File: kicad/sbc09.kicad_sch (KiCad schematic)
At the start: 77 parts, among them J1 Conn_01x04_Male, J2 Conn_01x06_Male, J3 Conn_01x06_Male, J4 Conn_01x06_Male, J5 Conn_02x05_Odd_Even, J6 Conn_02x25_Odd_Even, J7 Conn_02x05_Odd_Even, Q1 2N7000, SW1 SW_Push, U1 74HCT245, U10 SST39SF040-DIP, U11 XR68C681CJ, U12 MAX232, U2 74HCT245, U3 74HCT245, U4 MC6809E, U5 74HCT125, U6 EPM7128SLC84, U7 71256SA15TPG, U8 AS6C4008-55PCN, U9 SST39SF040-DIP, X1 8MHz, X2 3.6864MHz

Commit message: KiCAD: Replace 74HCT125 with 74HCT32 and add INTMASK from CPLD
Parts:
- removed U5: 74HCT125, Package_DIP:DIP-14_W7.62mm_Socket, symbol 74xx:74LS125
- added U5: 74HCT32, Package_DIP:DIP-14_W7.62mm_Socket, symbol 74xx:74LS32
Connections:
- net A3: no longer U6.21 (A3)
- net CLKX4: now also U5.4
- net CLKX4Bus: now also U5.6
- net E: now also U6.8 (EX), U5.1
- net EBus: now also U5.3
- net GND: now also U5.2, U5.5, U5.7 (GND)
- net Q: now also U6.5 (QX)
- net VCC: now also U5.14 (VCC)
- net nENCLK: now also U6.6 (ENCLK)
- net nFIRQ: now also U5.13; no longer U4.4 (~{FIRQ})
- net nIRQ: now also U5.9; no longer U4.3 (~{IRQ})
- new net: U4.4 (~{FIRQ}), U5.11
- new net: U4.3 (~{IRQ}), U5.8
- new net INTMASK: U5.10, U5.12, U6.21 (INTMASK)
- no-connect marks 22 -> 21
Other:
- note added: "NOTE: Could save a pin by combining EX and E."
- moved on the sheet: RN1

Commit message: KiCAD: Connect SD Card to CPLD
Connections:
- net GND: now also U7.3 (A7), U7.4 (A6), U7.5 (A5)
- net SDCLK: now also U6.73 (SCLK); no longer U11.29 (OP6)
- net SDCS: now also U11.17 (OP7); no longer U11.16 (OP5)
- net SDMISO: now also U6.74 (MISO); no longer U11.42 (IP5)
- net SDMOSI: now also U6.76 (MOSI); no longer U11.17 (OP7)
- removed net MMU_A5: U6.73 (MMU_A5), U7.5 (A5)
- removed net MMU_A6: U6.76 (MMU_A6), U7.4 (A6)
- removed net MMU_A7: U6.74 (MMU_A7), U7.3 (A7)
- no-connect marks 21 -> 24
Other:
- moved on the sheet: J4

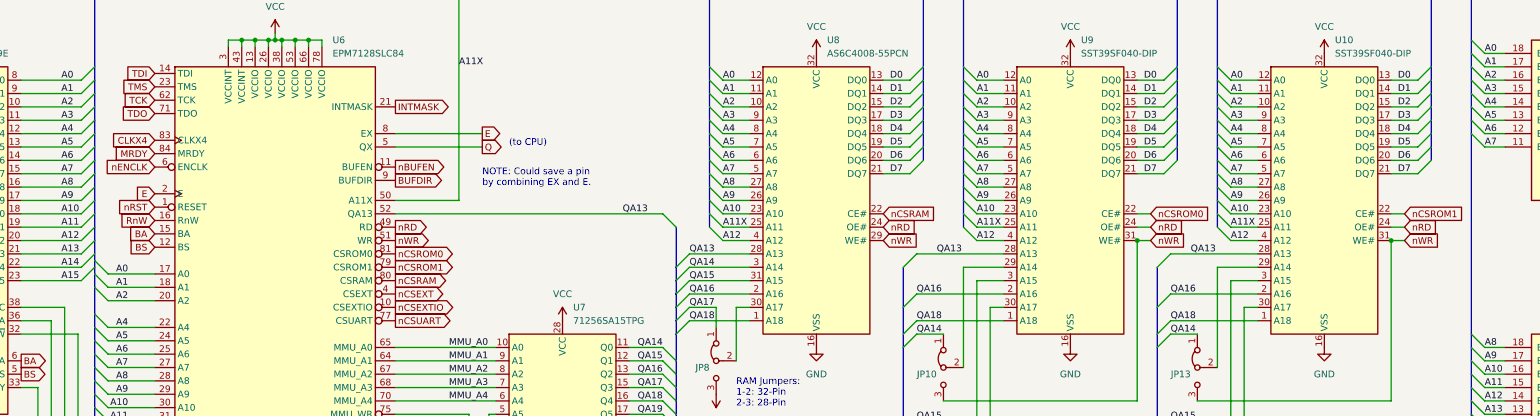
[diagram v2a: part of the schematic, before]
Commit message: KiCAD: Re-instate ADDR3 at the expense of seperate nRD/nWR signals
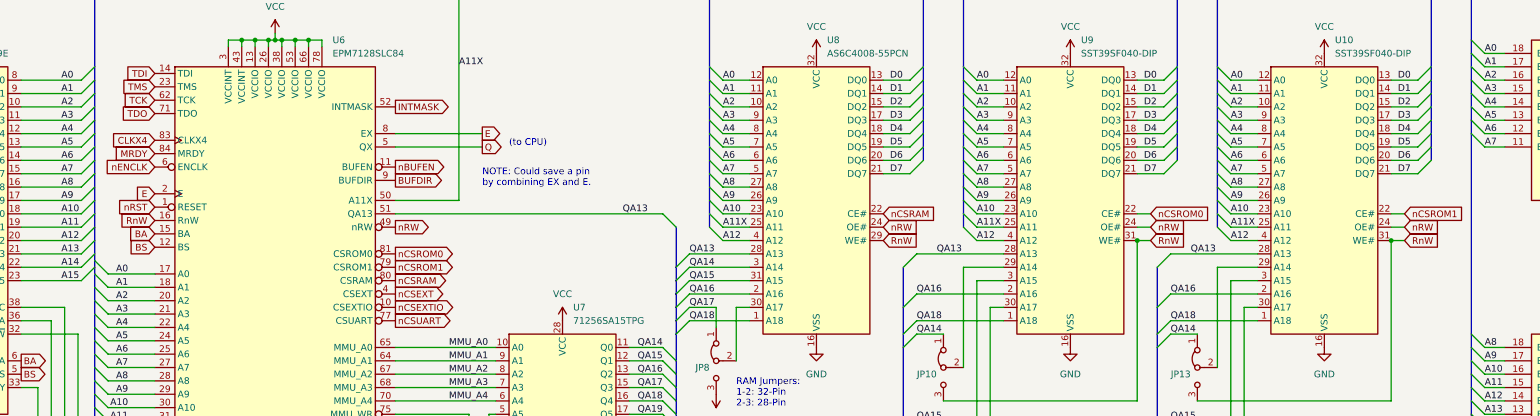
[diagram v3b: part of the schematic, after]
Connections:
- net A3: now also U6.21 (A3)
- net INTMASK: now also U6.52 (INTMASK); no longer U6.21 (INTMASK)
- net QA13: now also U6.51 (QA13); no longer U6.52 (QA13)
- net RnW: now also JP10.3 (B), JP13.3 (B), U10.31 (WE#), U8.29 (WE#), U9.31 (WE#)
- net nRD renamed nRW
- removed net nWR: JP10.3 (B), JP13.3 (B), U10.31 (WE#), U6.51 (WR), U8.29 (WE#), U9.31 (WE#)
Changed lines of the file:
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@@
     (stroke (width 0) (type default) (color 0 0 0 0))
   )
+  (bus_entry (at 93.98 85.09) (size -2.54 -2.54)
+    (stroke (width 0) (type default) (color 0 0 0 0))
+  )
   (bus_entry (at 201.93 76.2) (size 2.54 -2.54)
     (stroke (width 0) (type default) (color 0 0 0 0))
@@
     (stroke (width 0) (type default) (color 0 0 0 0))
   )
+  (wire (pts (xy 93.98 85.09) (xy 102.87 85.09))
+    (stroke (width 0) (type default) (color 0 0 0 0))
+  )
   (wire (pts (xy 77.47 40.64) (xy 88.9 40.64))
     (stroke (width 0) (type default) (color 0 0 0 0))
@@
     (stroke (width 0) (type default) (color 0 0 0 0))
   )
-  (bus (pts (xy 91.44 80.01) (xy 91.44 85.09))
+  (bus (pts (xy 91.44 80.01) (xy 91.44 82.55))
     (stroke (width 0) (type default) (color 0 0 0 0))
   )
@@
     (stroke (width 0) (type default) (color 0 0 0 0))
   )
+  (bus (pts (xy 91.44 82.55) (xy 91.44 85.09))
+    (stroke (width 0) (type default) (color 0 0 0 0))
+  )
   (wire (pts (xy 45.72 53.34) (xy 52.07 53.34))
     (stroke (width 0) (type default) (color 0 0 0 0))
@@
     (effects (font (size 1.27 1.27)) (justify left bottom))
   )
+  (label "A3" (at 97.79 85.09 180)
+    (effects (font (size 1.27 1.27)) (justify right bottom))
+  )
   (label "A6" (at 307.34 55.88 0)
     (effects (font (size 1.27 1.27)) (justify left bottom))
@@
     )
   )
-  (global_label "nWR" (shape input) (at 340.36 71.12 0) (fields_autoplaced)
+  (global_label "RnW" (shape input) (at 340.36 71.12 0) (fields_autoplaced)
     (effects (font (size 1.27 1.27)) (justify left))
     (property "Intersheet References" "${INTERSHEET_REFS}" (id 0) (at 346.6436 71.0406 0)
@@
     )
   )
-  (global_label "nRD" (shape output) (at 148.59 68.58 0) (fields_autoplaced)
+  (global_label "nRW" (shape output) (at 148.59 68.58 0) (fields_autoplaced)
     (effects (font (size 1.27 1.27)) (justify left))
-    (property "Intersheet References" "${INTERSHEET_REFS}" (id 0) (at 154.6921 68.5006 0)
+    (property "Intersheet References" "${INTERSHEET_REFS}" (id 0) (at 154.8736 68.5006 0)
       (effects (font (size 1.27 1.27)) (justify left) hide)
     )
@@
     )
   )
-  (global_label "nRD" (shape input) (at 292.1 68.58 0) (fields_autoplaced)
+  (global_label "nRW" (shape input) (at 292.1 68.58 0) (fields_autoplaced)
     (effects (font (size 1.27 1.27)) (justify left))
-    (property "Intersheet References" "${INTERSHEET_REFS}" (id 0) (at 298.2021 68.5006 0)
+    (property "Intersheet References" "${INTERSHEET_REFS}" (id 0) (at 298.3836 68.5006 0)
       (effects (font (size 1.27 1.27)) (justify left) hide)
     )
@@
     )
   )
-  (global_label "nRD" (shape input) (at 340.36 68.58 0) (fields_autoplaced)
+  (global_label "nRW" (shape input) (at 340.36 68.58 0) (fields_autoplaced)
     (effects (font (size 1.27 1.27)) (justify left))
-    (property "Intersheet References" "${INTERSHEET_REFS}" (id 0) (at 346.4621 68.5006 0)
+    (property "Intersheet References" "${INTERSHEET_REFS}" (id 0) (at 346.6436 68.5006 0)
       (effects (font (size 1.27 1.27)) (justify left) hide)
     )
@@
     )
   )
-  (global_label "nRD" (shape input) (at 241.3 68.58 0) (fields_autoplaced)
+  (global_label "nRW" (shape input) (at 241.3 68.58 0) (fields_autoplaced)
     (effects (font (size 1.27 1.27)) (justify left))
-    (property "Intersheet References" "${INTERSHEET_REFS}" (id 0) (at 247.4021 68.5006 0)
+    (property "Intersheet References" "${INTERSHEET_REFS}" (id 0) (at 247.5836 68.5006 0)
       (effects (font (size 1.27 1.27)) (justify left) hide)
     )
@@
     )
   )
-  (global_label "nWR" (shape input) (at 292.1 71.12 0) (fields_autoplaced)
+  (global_label "RnW" (shape input) (at 292.1 71.12 0) (fields_autoplaced)
     (effects (font (size 1.27 1.27)) (justify left))
     (property "Intersheet References" "${INTERSHEET_REFS}" (id 0) (at 298.3836 71.0406 0)
@@
     )
   )
-  (global_label "nWR" (shape input) (at 241.3 71.12 0) (fields_autoplaced)
+  (global_label "RnW" (shape input) (at 241.3 71.12 0) (fields_autoplaced)
     (effects (font (size 1.27 1.27)) (justify left))
     (property "Intersheet References" "${INTERSHEET_REFS}" (id 0) (at 247.5836 71.0406 0)
       (effects (font (size 1.27 1.27)) (justify left) hide)
     )
-  )
-  (global_label "nWR" (shape output) (at 148.59 71.12 0) (fields_autoplaced)
-    (effects (font (size 1.27 1.27)) (justify left))
-    (property "Intersheet References" "${INTERSHEET_REFS}" (id 0) (at 154.8736 71.0406 0)
-      (effects (font (size 1.27 1.27)) (justify left) hide)
-    )

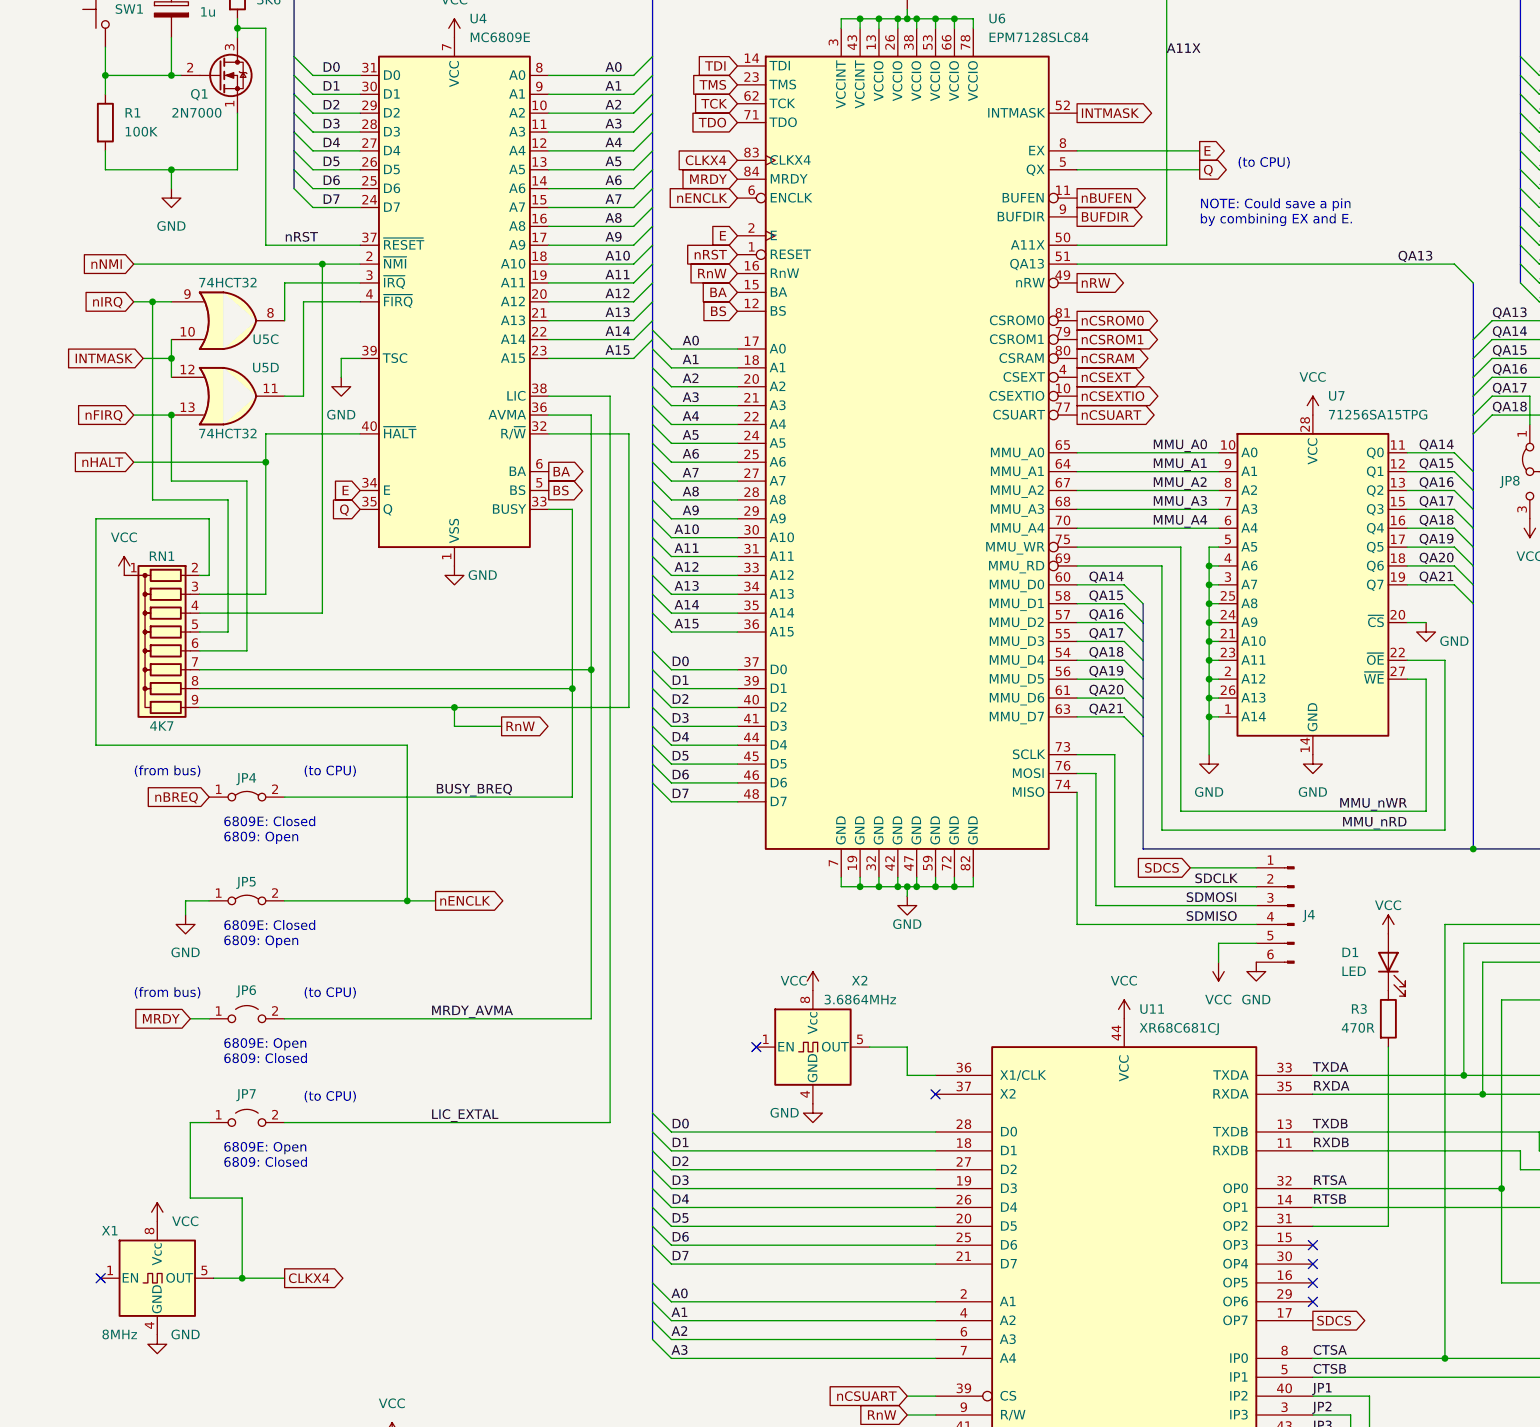
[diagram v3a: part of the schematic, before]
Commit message: KiCAD: Merge E and EX clocks, add JP16 for spare input
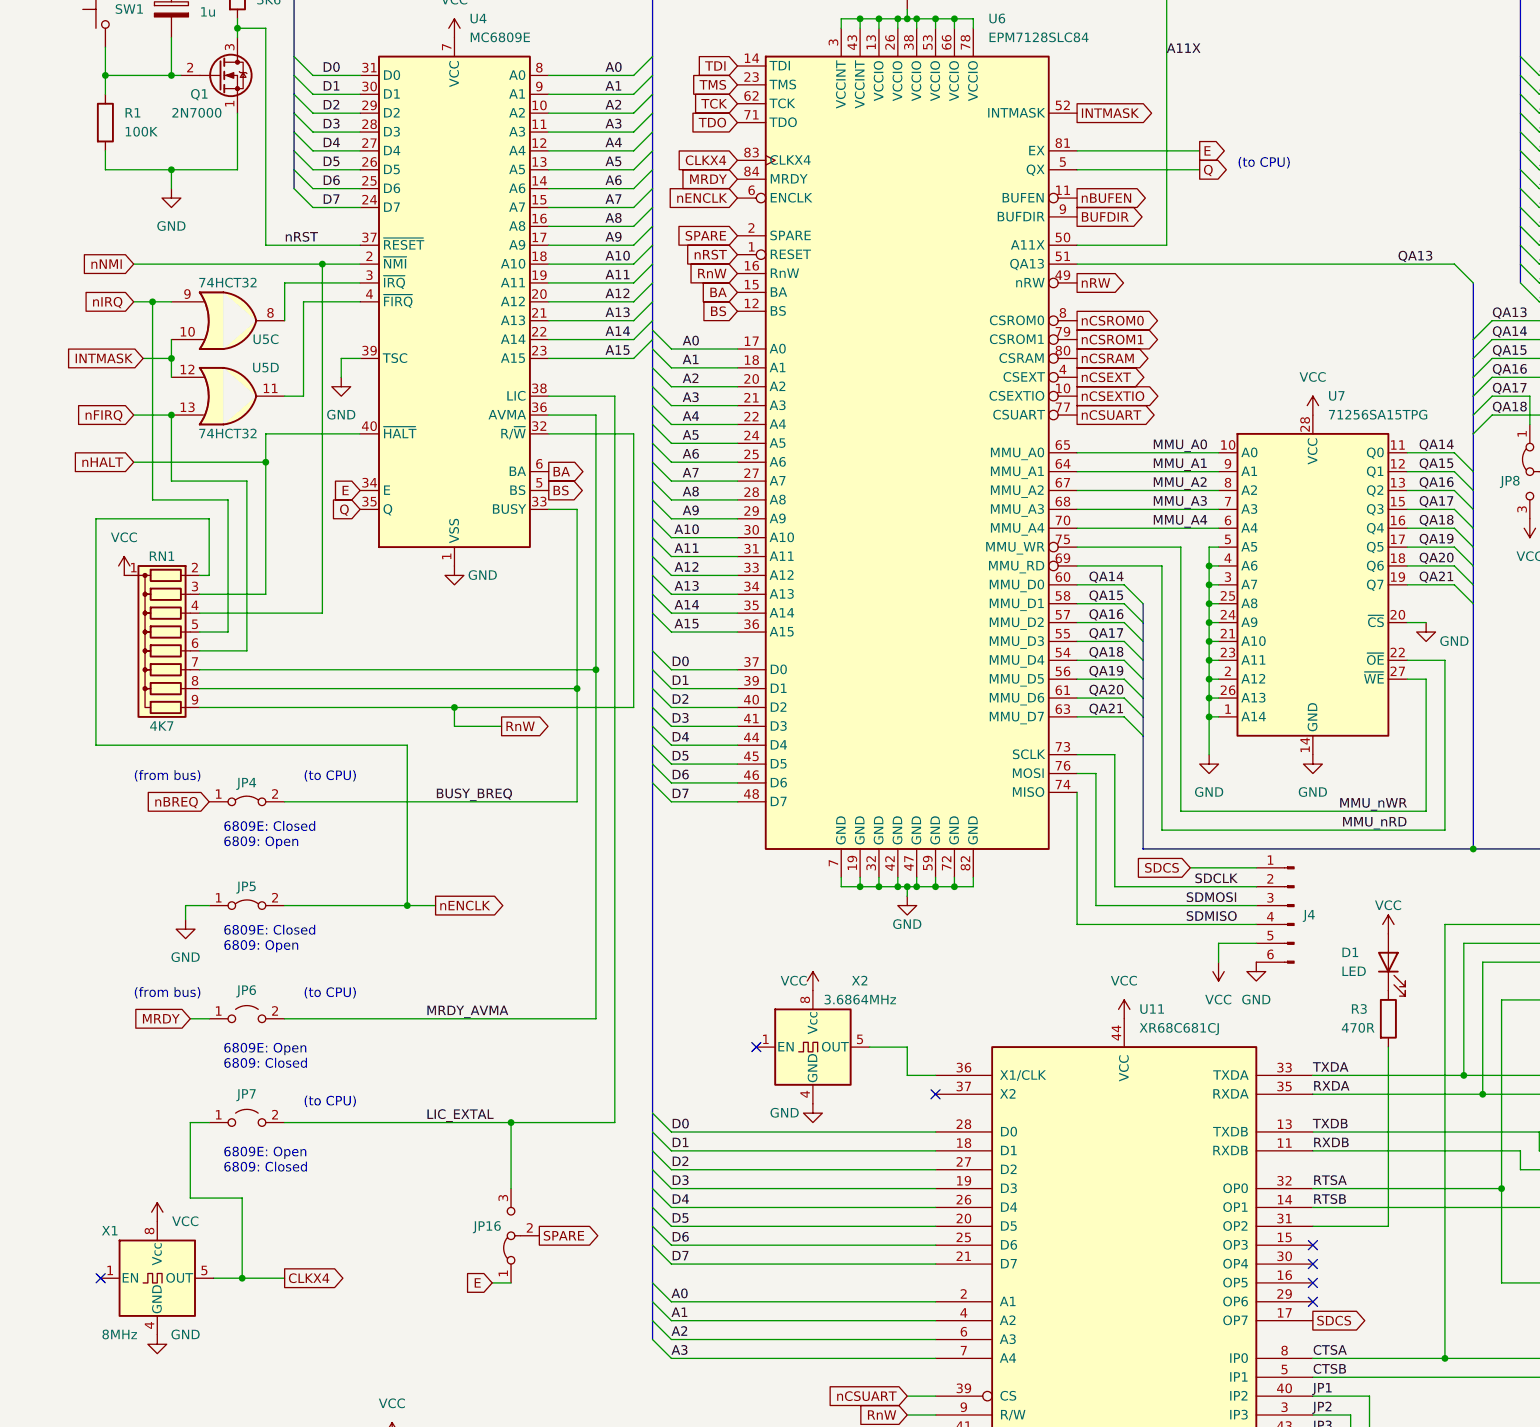
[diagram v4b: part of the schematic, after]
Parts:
- added JP16: Jumper_3_Bridged12, Connector_PinHeader_2.54mm:PinHeader_1x03_P2.54mm_Vertical, symbol Jumper:Jumper_3_Bridged12
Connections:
- net E: now also U6.81 (EX), JP16.1 (A); no longer U6.2 (E), U6.8 (EX)
- net LIC_EXTAL: now also JP16.3 (B)
- net nCSROM0: now also U6.8 (CSROM0); no longer U6.81 (CSROM0)
- new net SPARE: JP16.2 (C), U6.2 (SPARE)
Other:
- note removed: "NOTE: Could save a pin by combining EX and E."
- moved on the sheet: JP4, JP5
